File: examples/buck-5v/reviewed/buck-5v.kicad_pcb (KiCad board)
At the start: 2 copper layers, 126 x 56 mm, 11 parts, among them J1 12V IN, J2 5V OUT, U1 LM2596S-5

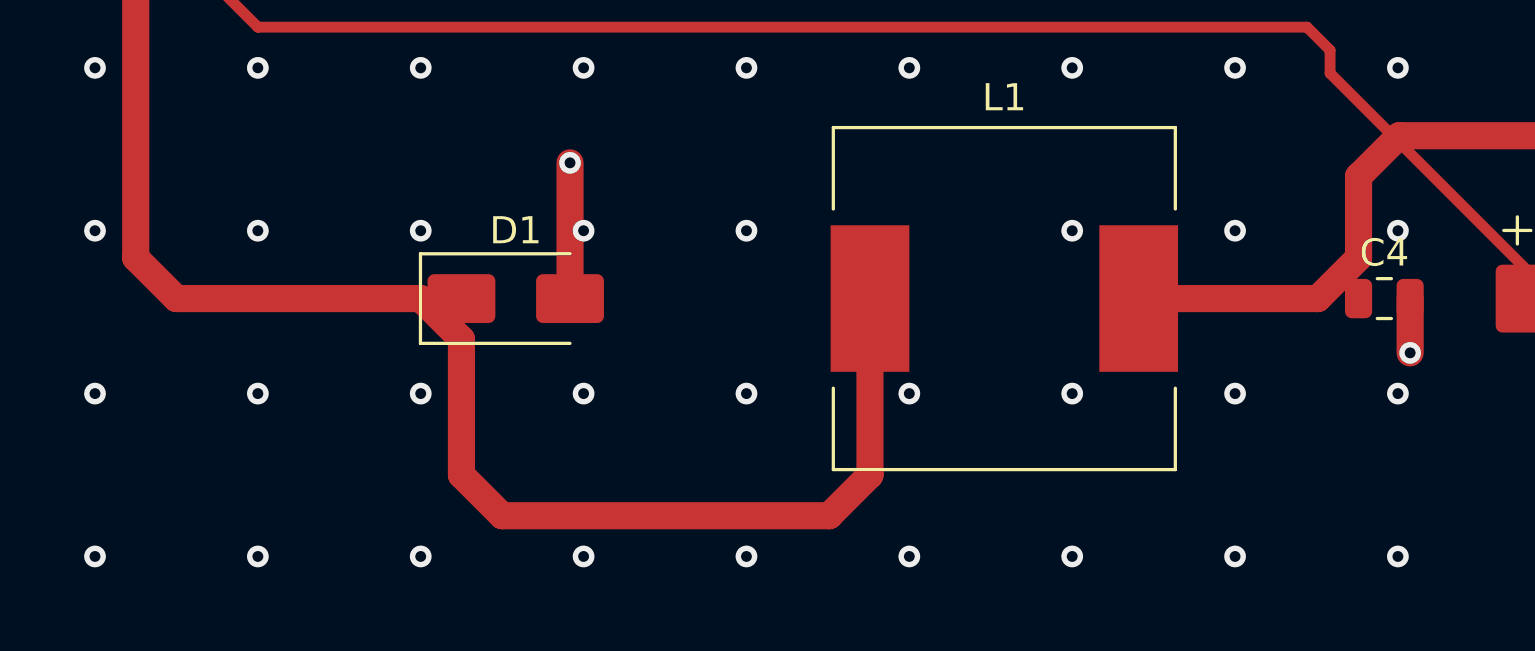
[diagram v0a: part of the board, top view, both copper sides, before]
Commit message: Never cut a corner off the pad it was there to reach
Once two routes meeting at a pad are merged into one run, the pad is an
interior corner of a polyline like any other, and the chamfer cut it -
moving the copper off the pad and leaving the net unconnected, which is
not something you can see in the shape. Both clean-up passes now hold
every pad and every track end still, from one list, for the same reason:
copper that something else is joined to is not theirs to move.

That is the last of the unconnected-net errors on the buck, the motor
and the opamp boards, and the 0 degree spur on the Pico's VSYS - which
was the failed half of a route to a pad the chamfer had already cut it
away from.
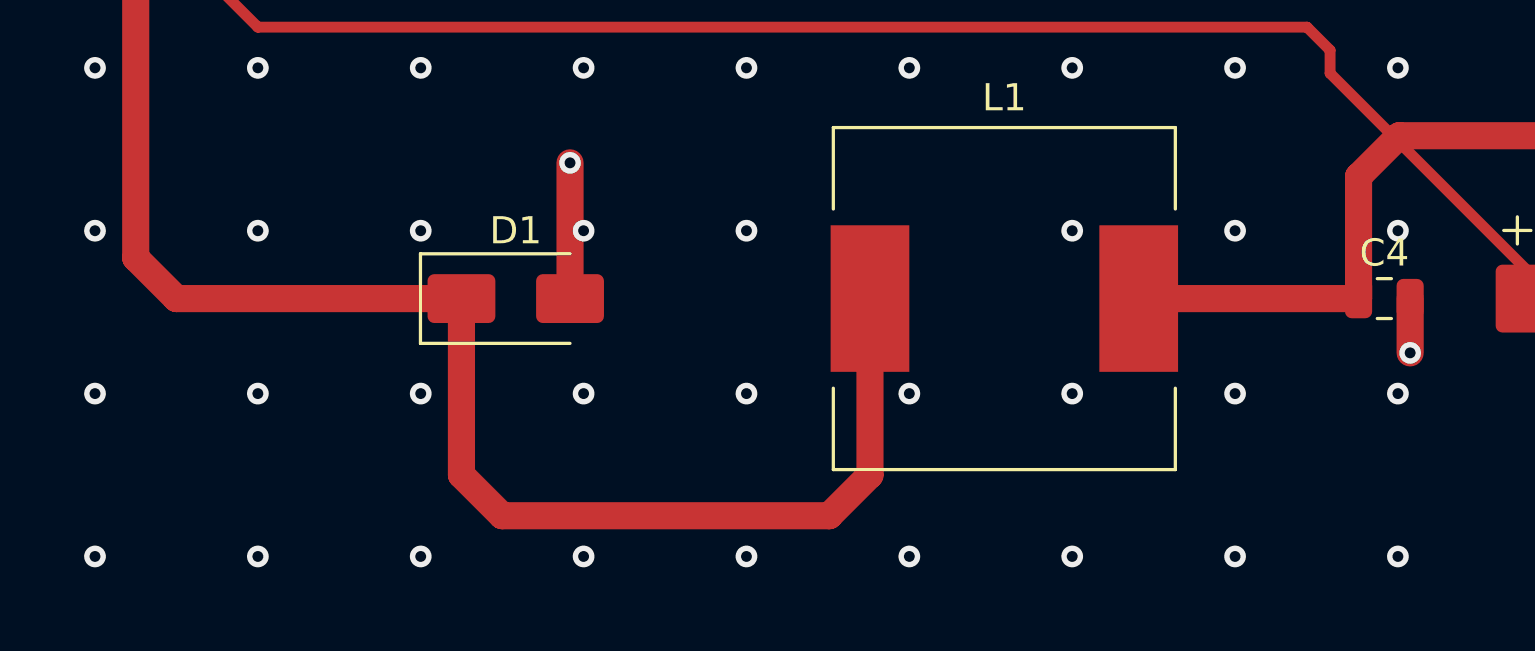
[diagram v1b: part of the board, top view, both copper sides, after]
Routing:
- net /SW: track 74.7 -> 75.6 mm
- net /+5V: track 141.0 -> 141.9 mm
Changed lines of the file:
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@@
 	(segment (start 144.0 71.8) (end 144.0 94.5) (width 1.0) (layer "F.Cu") (net 5))
 	(segment (start 144.0 94.5) (end 145.5 96.0) (width 1.0) (layer "F.Cu") (net 5))
-	(segment (start 145.5 96.0) (end 154.5 96.0) (width 1.0) (layer "F.Cu") (net 5))
-	(segment (start 154.5 96.0) (end 156.0 97.5) (width 1.0) (layer "F.Cu") (net 5))
-	(segment (start 156.0 97.5) (end 156.0 102.5) (width 1.0) (layer "F.Cu") (net 5))
+	(segment (start 145.5 96.0) (end 156.0 96.0) (width 1.0) (layer "F.Cu") (net 5))
+	(segment (start 156.0 96.0) (end 156.0 102.5) (width 1.0) (layer "F.Cu") (net 5))
 	(segment (start 156.0 102.5) (end 157.5 104.0) (width 1.0) (layer "F.Cu") (net 5))
 	(segment (start 157.5 104.0) (end 169.55 104.0) (width 1.0) (layer "F.Cu") (net 5))
@@
 	(segment (start 188.0 86.85) (end 188.0 87.7) (width 0.4) (layer "F.Cu") (net 3))
 	(segment (start 188.0 87.7) (end 196.3 96.0) (width 0.4) (layer "F.Cu") (net 3))
-	(segment (start 180.95 96.0) (end 187.55 96.0) (width 1.0) (layer "F.Cu") (net 3))
-	(segment (start 187.55 96.0) (end 189.05 94.5) (width 1.0) (layer "F.Cu") (net 3))
-	(segment (start 189.05 94.5) (end 189.05 91.5) (width 1.0) (layer "F.Cu") (net 3))
+	(segment (start 180.95 96.0) (end 189.05 96.0) (width 1.0) (layer "F.Cu") (net 3))
+	(segment (start 189.05 96.0) (end 189.05 91.5) (width 1.0) (layer "F.Cu") (net 3))
 	(segment (start 189.05 91.5) (end 190.55 90.0) (width 1.0) (layer "F.Cu") (net 3))
 	(segment (start 190.55 90.0) (end 196.3 90.0) (width 1.0) (layer "F.Cu") (net 3))
